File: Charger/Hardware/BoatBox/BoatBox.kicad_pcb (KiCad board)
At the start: 2 copper layers, 97.2 x 86.3 mm, 154 parts, among them P101 TestPoint, P102 TestPoint, P103 TestPoint, P104 TestPoint, P105 TestPoint, P106 TestPoint, P107 TestPoint, P108 TestPoint, P109 TestPoint, P110 TestPoint, P111 TestPoint, P112 TestPoint, P113 TestPoint, P114 TestPoint, P115 TestPoint, P116 TestPoint, P117 TestPoint, P118 TestPoint, P119 TestPoint, P120 TestPoint, P201 TestPoint, P202 TestPoint, P301 TestPoint, P302 TestPoint, P401 TestPoint, P402 TestPoint, P501 TestPoint, P502 TestPoint, T101 IRFR5505PBF, T102 BSS138, T103 IRFR5505PBF, T201 BC847, T202 IPD50R380CE, T203 BSS138, T301 BC847, T302 IPD50R380CE, T303 BSS138, T401 BC847, T402 IPD50R380CE, T403 BSS138, T501 BC847, T502 IPD50R380CE, T503 BSS138, X101 HCCPHPE24BKA90F

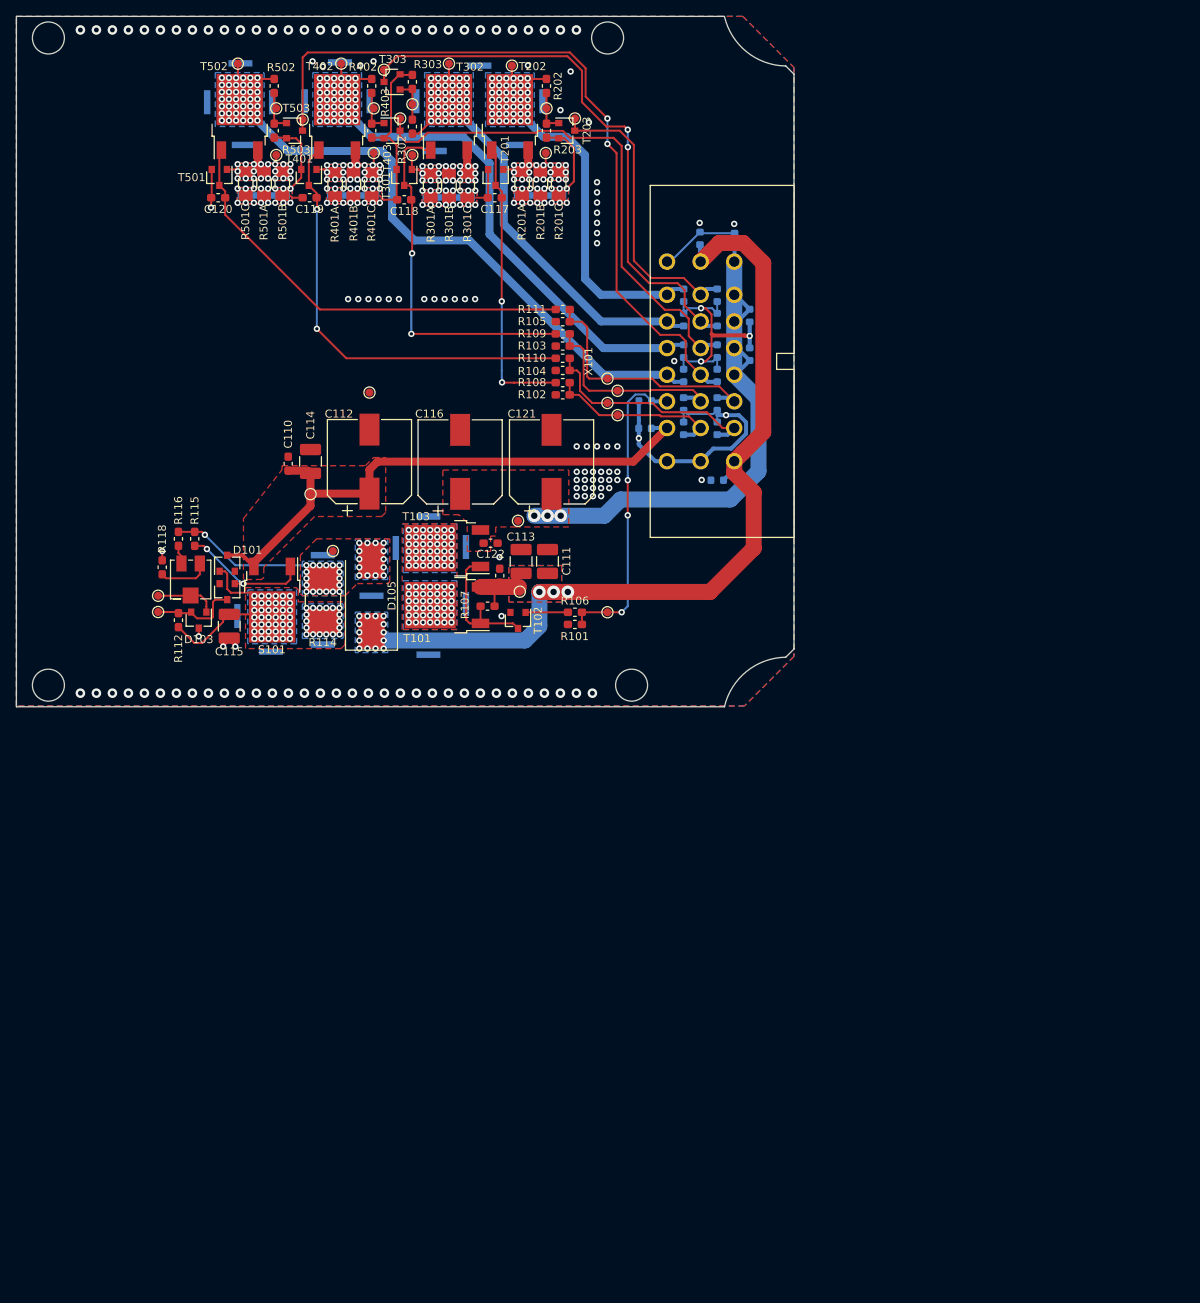
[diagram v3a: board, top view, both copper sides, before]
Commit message: Start to create the new pcb
Main features in this revision shall be:
 -) 3D printed housing
 -) raised aluminium inlay for heat transfer
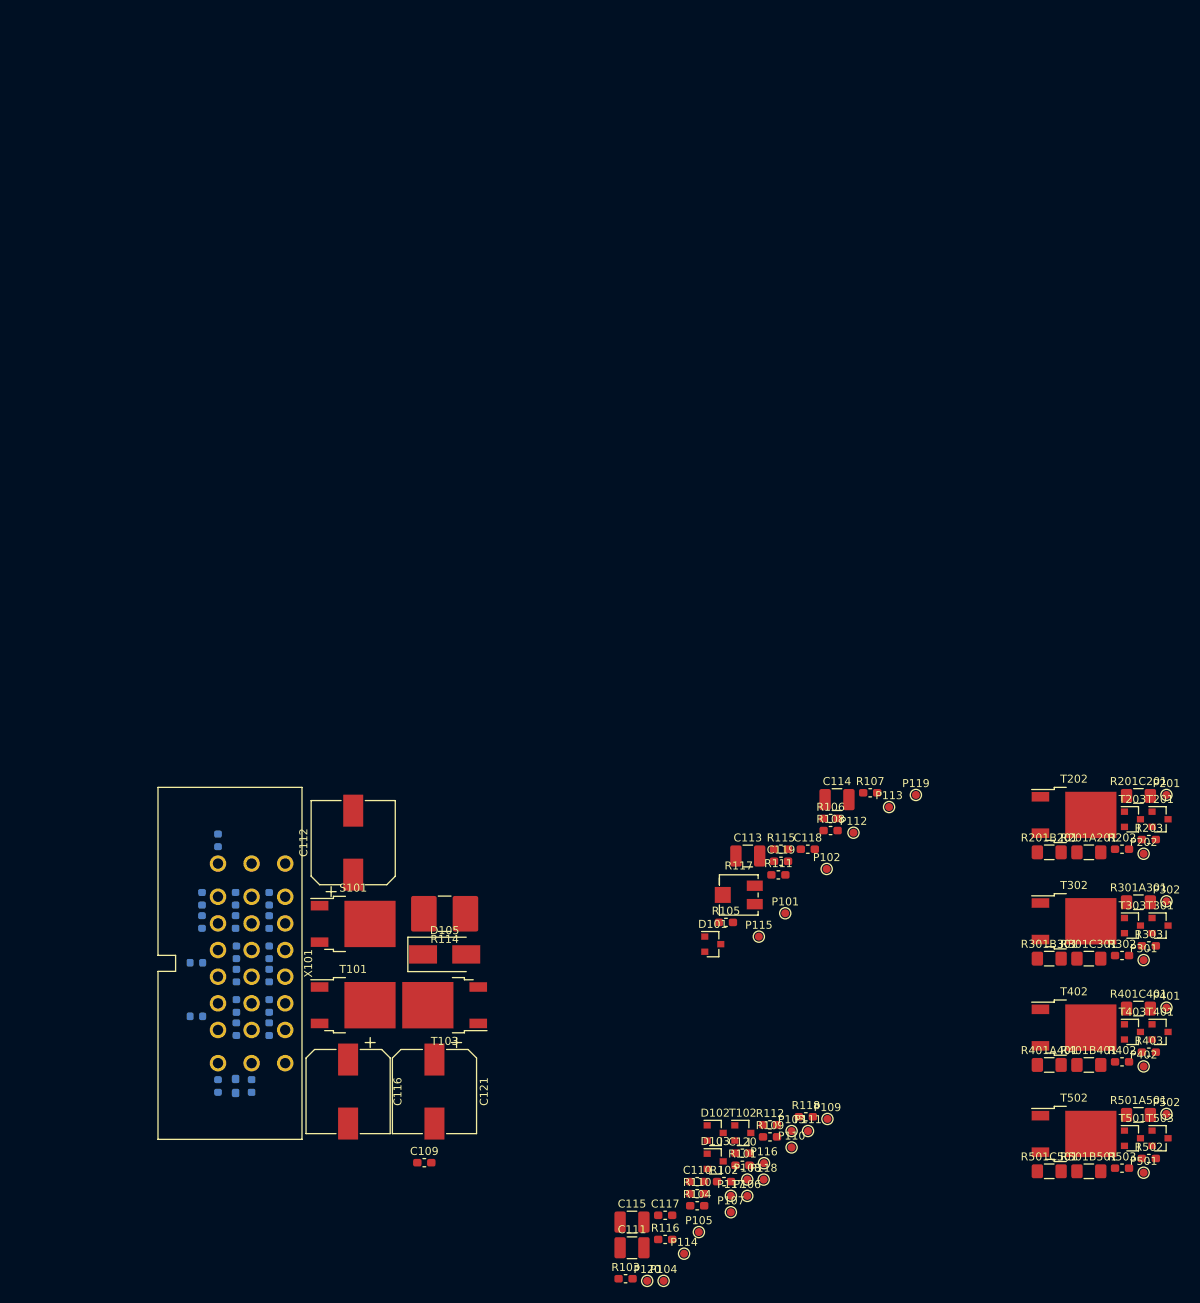
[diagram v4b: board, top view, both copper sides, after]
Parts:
- removed ?: , boatbox:Zeichnung
- removed C101, C102, C103, C104, C105, C106, C107, C108, C124, C125, C126, C127, C128, C129, C130, C131, C132, C133, C134: 4.7n, Capacitor_SMD:C_0603_1608Metric
- removed R201A, R201B, R201C, R301A, R301B, R301C, R401A, R401B, R401C, R501A, R501B, R501C: 1R, Resistor_SMD:R_1206_3216Metric_Pad1.42x1.75mm_HandSolder
- removed REF** (x30): BUMP-SR0.8-3.0, boatbox:BUMP-SR0.8-3.0
- removed REF** (x4): MountingHole_4mm, MountingHole:MountingHole_4mm
- added C0A1: 4.7n, Capacitor_SMD:C_0603_1608Metric, B.Cu at (186.2, 169.4)
- added C0A2: 4.7n, Capacitor_SMD:C_0603_1608Metric, B.Cu at (184.2, 176.7)
- added C0A3: 4.7n, Capacitor_SMD:C_0603_1608Metric, B.Cu at (184.2, 179.6)
- added C0A5: 4.7n, Capacitor_SMD:C_0603_1608Metric, B.Cu at (183.5, 184.7)
- added C0A7: 4.7n, Capacitor_SMD:C_0603_1608Metric, B.Cu at (183.5, 191.4)
- added C0A8: 4.7n, Capacitor_SMD:C_0603_1608Metric, B.Cu at (186.2, 200.1)
- added C0B2: 4.7n, Capacitor_SMD:C_0603_1608Metric, B.Cu at (188.4, 176.7)
- added C0B3: 4.7n, Capacitor_SMD:C_0603_1608Metric, B.Cu at (188.4, 179.6)
- added C0B4: 4.7n, Capacitor_SMD:C_0603_1608Metric, B.Cu at (188.5, 183.4)
- added C0B5: 4.7n, Capacitor_SMD:C_0603_1608Metric, B.Cu at (188.5, 186.3)
- added C0B6: 4.7n, Capacitor_SMD:C_0603_1608Metric, B.Cu at (188.5, 190.1)
- added C0B7: 4.7n, Capacitor_SMD:C_0603_1608Metric, B.Cu at (188.5, 193.0)
- added C0B8: 4.7n, Capacitor_SMD:C_0603_1608Metric, B.Cu at (190.4, 200.1)
- added C0C2: 4.7n, Capacitor_SMD:C_0603_1608Metric, B.Cu at (192.6, 176.7)
- added C0C3: 4.7n, Capacitor_SMD:C_0603_1608Metric, B.Cu at (192.6, 179.6)
- added C0C4: 4.7n, Capacitor_SMD:C_0603_1608Metric, B.Cu at (192.6, 183.4)
- added C0C5: 4.7n, Capacitor_SMD:C_0603_1608Metric, B.Cu at (192.6, 186.3)
- added C0C6: 4.7n, Capacitor_SMD:C_0603_1608Metric, B.Cu at (192.6, 190.1)
- added C0C7: 4.7n, Capacitor_SMD:C_0603_1608Metric, B.Cu at (192.6, 193.0)
- added R201A201: 1R, Resistor_SMD:R_1206_3216Metric_Pad1.42x1.75mm_HandSolder, F.Cu at (295.0, 170.9)
- added R201B201: 1R, Resistor_SMD:R_1206_3216Metric_Pad1.42x1.75mm_HandSolder, F.Cu at (290.1, 170.9)
- added R201C201: 1R, Resistor_SMD:R_1206_3216Metric_Pad1.42x1.75mm_HandSolder, F.Cu at (301.2, 163.8)
- added R301A301: 1R, Resistor_SMD:R_1206_3216Metric_Pad1.42x1.75mm_HandSolder, F.Cu at (301.2, 177.1)
- added R301B301: 1R, Resistor_SMD:R_1206_3216Metric_Pad1.42x1.75mm_HandSolder, F.Cu at (290.1, 184.1)
- added R301C301: 1R, Resistor_SMD:R_1206_3216Metric_Pad1.42x1.75mm_HandSolder, F.Cu at (295.0, 184.1)
- added R401A401: 1R, Resistor_SMD:R_1206_3216Metric_Pad1.42x1.75mm_HandSolder, F.Cu at (290.1, 197.4)
- added R401B401: 1R, Resistor_SMD:R_1206_3216Metric_Pad1.42x1.75mm_HandSolder, F.Cu at (295.0, 197.4)
- added R401C401: 1R, Resistor_SMD:R_1206_3216Metric_Pad1.42x1.75mm_HandSolder, F.Cu at (301.2, 190.4)
- added R501A501: 1R, Resistor_SMD:R_1206_3216Metric_Pad1.42x1.75mm_HandSolder, F.Cu at (301.2, 203.7)
- added R501B501: 1R, Resistor_SMD:R_1206_3216Metric_Pad1.42x1.75mm_HandSolder, F.Cu at (295.0, 210.7)
- added R501C501: 1R, Resistor_SMD:R_1206_3216Metric_Pad1.42x1.75mm_HandSolder, F.Cu at (290.1, 210.7)
- C122: moved to B.Cu
- D105: footprint Diode_SMD:D_SMC_Handsoldering -> Diode_SMD:D_SMB_Handsoldering
- moved R502 173.0 mm to (302.5, 209.1), turned to 0 degrees
- moved P502 167.9 mm to (304.7, 203.6), turned to 0 degrees
- moved R503 167.5 mm to (299.2, 210.3), turned to 0 degrees
- moved P501 167.1 mm to (301.9, 210.9), turned to 0 degrees
- moved T503 166.0 mm to (303.9, 206.6)
- moved T501 165.7 mm to (300.5, 206.6), turned to 0 degrees
- moved T502 164.5 mm to (293.2, 206.1), turned to 0 degrees
- moved P120 160.5 mm to (239.8, 224.4), turned to 0 degrees
- moved R402 153.9 mm to (299.2, 197.0), turned to 0 degrees
- moved P402 153.6 mm to (301.9, 197.6), turned to 0 degrees
- moved T401 150.8 mm to (303.9, 193.3), turned to 0 degrees
- moved R403 150.7 mm to (302.5, 195.8), turned to 0 degrees
- moved P114 150.1 mm to (244.4, 221.0), turned to 0 degrees
- moved P118 149.2 mm to (254.4, 211.8), turned to 0 degrees
- moved T402 146.5 mm to (293.2, 192.8), turned to 0 degrees
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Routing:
- net GND: track 134.5 -> 0.00 mm, vias 198 -> 0
- net UBD: track 120.2 -> 0.00 mm, vias 17 -> 0
- net /A_S_DIAG4: track 93.7 -> 0.00 mm, vias 2 -> 0
- net /A_T_OUT4: track 77.7 -> 0.00 mm, vias 42 -> 0
- net /U_U_CHRG: track 73.2 -> 0.00 mm
- net /A_S_DIAG2: track 71.0 -> 0.00 mm, vias 2 -> 0
- net UBR: track 70.3 -> 0.00 mm, vias 3 -> 0
- net /A_S_DIAG3: track 64.2 -> 0.00 mm
- net /A_T_OUT3: track 62.1 -> 0.00 mm, vias 42 -> 0
- net /LSS 3/ctrl: track 54.8 -> 0.00 mm, vias 2 -> 0
- net /LSS 4/ctrl: track 54.7 -> 0.00 mm
- net /A_T_OUT1: track 48.2 -> 0.00 mm, vias 42 -> 0
- net /A_T_OUT2: track 47.6 -> 0.00 mm, vias 42 -> 0
- net /LSS 2/ctrl: track 45.5 -> 0.00 mm, vias 2 -> 0
- net /E_S_RLY: track 38.7 -> 0.00 mm, vias 3 -> 0
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- removed copper zone on B.Cu, net /A_T_OUT1
- removed copper zone on B.Cu, net /A_T_OUT2
- removed copper zone on B.Cu, net /A_T_OUT3
- removed copper zone on B.Cu, net /A_T_OUT4
- removed copper zone on F.Cu, net /U_U_CHRG
- removed copper zone on B.Cu, net GND
- removed copper zone on F.Cu, net GND
- removed copper zone on B.Cu, net Net-(C115-Pad1)
- removed copper zone on F.Cu, net Net-(C115-Pad1)
- removed copper zone on B.Cu, net Net-(D105-Pad2)
- removed copper zone on F.Cu, net Net-(D105-Pad2)
- removed copper zone on B.Cu, net Net-(P201-Pad1)
- removed copper zone on F.Cu, net Net-(P201-Pad1)
- removed copper zone on B.Cu, net Net-(P301-Pad1)
- removed copper zone on F.Cu, net Net-(P301-Pad1)
- removed copper zone on B.Cu, net Net-(P401-Pad1)
- removed copper zone on F.Cu, net Net-(P401-Pad1)
- removed copper zone on B.Cu, net Net-(P501-Pad1)
- removed copper zone on F.Cu, net Net-(P501-Pad1)
- removed copper zone on B.Cu, net Net-(T101-Pad2)
- removed copper zone on F.Cu, net Net-(T101-Pad2)
- removed copper zone on B.Cu, net UBD
- removed copper zone on F.Cu, net UBD
- removed copper zone on F.Cu, net UBR
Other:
- board outline removed

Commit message: WIP commit of new layout
squash after finish
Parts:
- added REF**: MountingHole_3.2mm_M3_Pad_Via, MountingHole:MountingHole_3.2mm_M3_Pad_Via, F.Cu at (245.0, 211.0)
- added REF**: MountingHole_3.2mm_M3_Pad_Via, MountingHole:MountingHole_3.2mm_M3_Pad_Via, F.Cu at (245.0, 159.0)
- added REF**: MountingHole_3.2mm_M3_Pad_Via, MountingHole:MountingHole_3.2mm_M3_Pad_Via, F.Cu at (183.0, 211.0)
- added REF**: MountingHole_3.2mm_M3_Pad_Via, MountingHole:MountingHole_3.2mm_M3_Pad_Via, F.Cu at (184.0, 159.0)
- C109, C110, R101, R106: moved to B.Cu
- moved P502 87.9 mm to (221.4, 175.6), turned to 270 degrees
- moved T503 87.4 mm to (223.0, 173.6), turned to 180 degrees
- moved T201 86.3 mm to (224.7, 200.8), turned to 180 degrees
- moved T501 85.7 mm to (223.0, 169.9), turned to 180 degrees
- moved R502 83.3 mm to (227.2, 173.6), turned to 270 degrees
- moved R503 82.3 mm to (225.6, 173.6), turned to 90 degrees
- moved R203 81.7 mm to (229.0, 204.8), turned to 270 degrees
- moved P202 81.3 mm to (227.2, 203.3), turned to 90 degrees
- moved P201 79.6 mm to (232.3, 196.7), turned to 90 degrees
- moved T203 78.8 mm to (231.5, 204.8)
- moved P501 77.3 mm to (229.5, 183.9), turned to 270 degrees
- moved R202 76.8 mm to (229.0, 201.5), turned to 270 degrees
- moved R107 72.6 mm to (200.7, 191.5), turned to 270 degrees
- moved R201C201 72.5 mm to (234.8, 193.0), turned to 90 degrees
- moved R401C401 72.5 mm to (230.5, 174.6), turned to 270 degrees
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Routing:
- net UBD: track 0.00 -> 91.4 mm
- net UBR: track 0.00 -> 91.1 mm, vias 0 -> 2
- net /A_T_OUT3: track 0.00 -> 67.5 mm, vias 0 -> 1
- net /A_T_OUT2: track 0.00 -> 64.3 mm
- net /A_T_OUT1: track 0.00 -> 45.5 mm, vias 0 -> 1
- net /U_U_CHRG: track 0.00 -> 38.6 mm, vias 0 -> 1
- net /A_T_OUT4: track 0.00 -> 36.1 mm
- net Net-(R107-Pad1): track 0.00 -> 29.5 mm
- net Net-(P501-Pad1): track 0.00 -> 28.4 mm, vias 0 -> 2
- net GND: track 0.00 -> 25.9 mm
- net /LSS 4/ctrl: track 0.00 -> 20.9 mm, vias 0 -> 2
- net /LSS 2/ctrl: track 0.00 -> 20.2 mm
- net Net-(R106-Pad2): track 0.00 -> 17.8 mm, vias 0 -> 3
- net Net-(P301-Pad1): track 0.00 -> 10.3 mm
- net /LSS 1/ctrl: track 0.00 -> 9.85 mm
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- added copper zone on B.Cu, net Net-(T101-Pad2)
- added copper zone on F.Cu, net Net-(T101-Pad2)
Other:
- board outline added: 70 x 60 mm

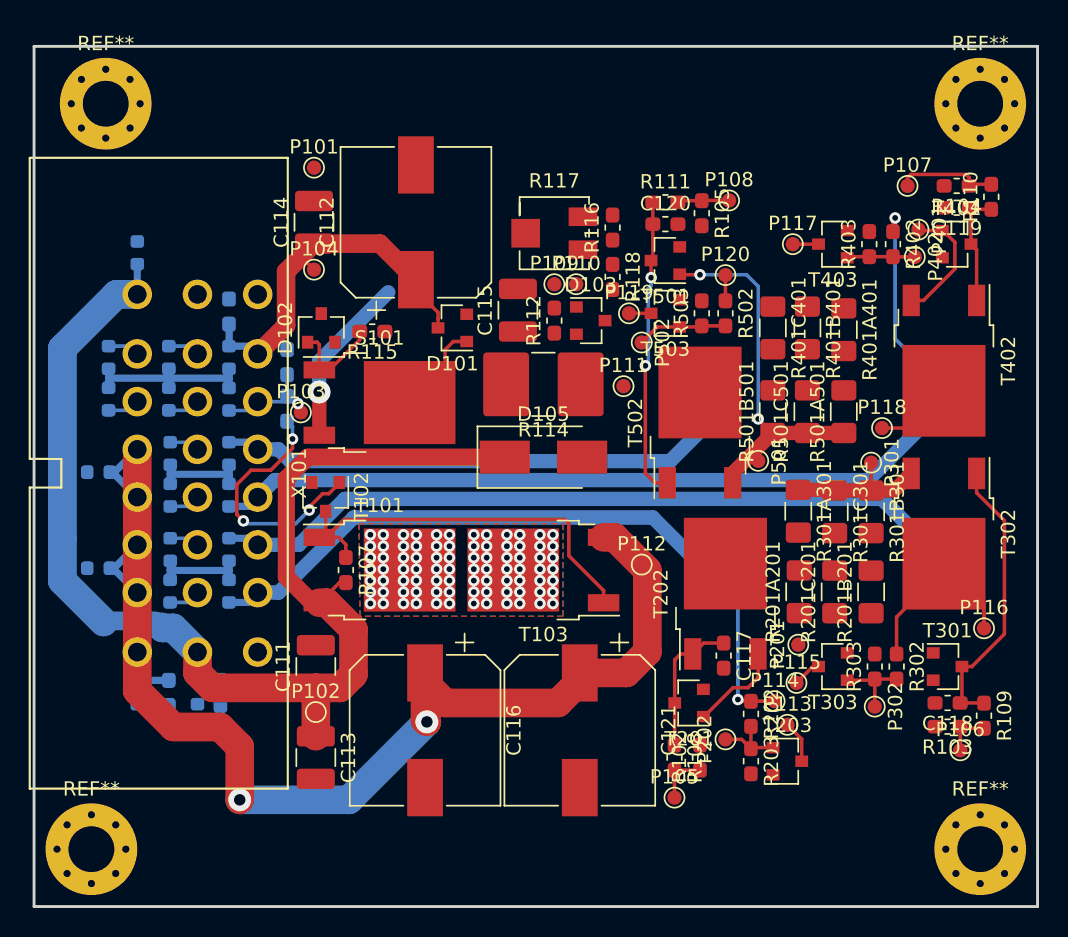
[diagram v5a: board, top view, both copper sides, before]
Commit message: New layout finished
Started work on the 3D printed housing. The cooling bench will be created
as an inlay made of 4mm steel (or aluminium).
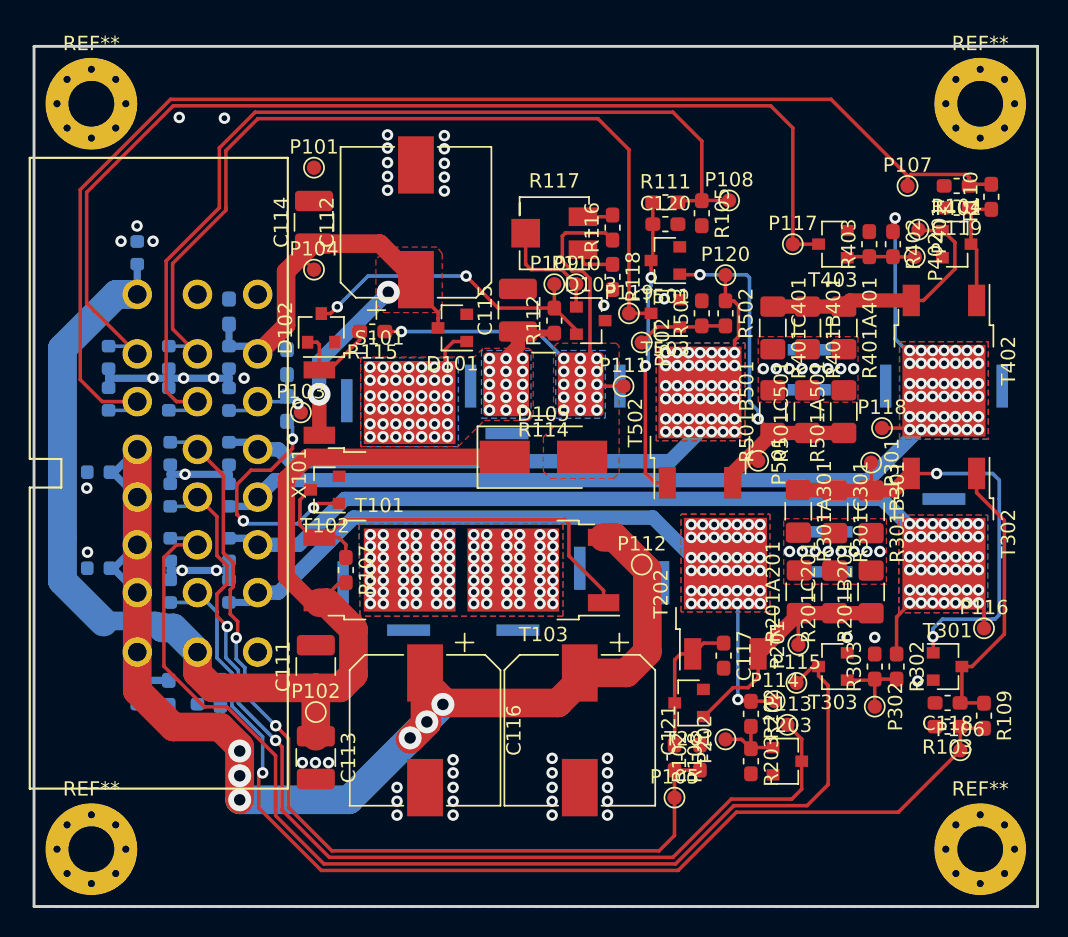
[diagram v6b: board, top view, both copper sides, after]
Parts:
- added REF**: BUMP-SR0.8-3.0, boatbox:BUMP-SR0.8-3.0, B.Cu at (200.5, 192.4)
- added REF**: BUMP-SR0.8-3.0, boatbox:BUMP-SR0.8-3.0, B.Cu at (217.1, 191.4)
- added REF**: BUMP-SR0.8-3.0, boatbox:BUMP-SR0.8-3.0, B.Cu at (233.1, 176.1)
- added REF**: BUMP-SR0.8-3.0, boatbox:BUMP-SR0.8-3.0, B.Cu at (233.1, 178.9)
- added REF**: BUMP-SR0.8-3.0, boatbox:BUMP-SR0.8-3.0, B.Cu at (234.6, 188.8)
- added REF**: BUMP-SR0.8-3.0, boatbox:BUMP-SR0.8-3.0, B.Cu at (234.6, 191.6)
- added REF**: BUMP-SR0.8-3.0, boatbox:BUMP-SR0.8-3.0, B.Cu at (222.9, 192.4)
- added REF**: BUMP-SR0.8-3.0, boatbox:BUMP-SR0.8-3.0, B.Cu at (242.5, 186.5)
- added REF**: BUMP-SR0.8-3.0, boatbox:BUMP-SR0.8-3.0, B.Cu at (238.4, 178.7)
- added REF**: BUMP-SR0.8-3.0, boatbox:BUMP-SR0.8-3.0, B.Cu at (246.5, 178.7)
- added REF**: BUMP-SR0.8-3.0, boatbox:BUMP-SR0.8-3.0, B.Cu at (209.4, 178.7)
- added REF**: BUMP-SR0.8-3.0, boatbox:BUMP-SR0.8-3.0, B.Cu at (212.0, 182.0)
- added REF**: BUMP-SR0.8-3.0, boatbox:BUMP-SR0.8-3.0, B.Cu at (219.8, 178.7)
- added REF**: BUMP-SR0.8-3.0, boatbox:BUMP-SR0.8-3.0, B.Cu at (200.8, 179.7)
- added REF**: BUMP-SR0.8-3.0, boatbox:BUMP-SR0.8-3.0, B.Cu at (212.7, 195.7)
- added REF**: BUMP-SR0.8-3.0, boatbox:BUMP-SR0.8-3.0, B.Cu at (205.1, 195.7)
- moved REF** 1.00 mm to (183.0, 159.0)
- moved T102 0.49 mm to (199.3, 185.9), turned to 180 degrees
- moved R401A401 0.13 mm to (235.5, 174.6)
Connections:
- C0A2 pad 2: /E_S_CTL3 -> /A_S_DIAG3
- C0A3 pad 2: /E_S_CTL4 -> /E_S_CTL3
- C0B2 pad 2: /E_S_CTL1 -> /A_S_DIAG4
- C0B3 pad 2: /E_S_CTL2 -> /E_S_CTL4
- C0B4 pad 2: /A_S_DIAG4 -> /E_S_CTL1
- C0B5 pad 2: /A_S_DIAG3 -> /A_S_DIAG1
- C0B7 pad 2: /A_S_DIAG1 -> /E_S_CTL2
- X101 pad 10: /E_S_CTL1 -> /A_S_DIAG4
- X101 pad 11: /E_S_CTL2 -> /E_S_CTL4
- X101 pad 12: /A_S_DIAG4 -> /E_S_CTL1
- X101 pad 13: /A_S_DIAG3 -> /A_S_DIAG1
- X101 pad 15: /A_S_DIAG1 -> /E_S_CTL2
- X101 pad 2: /E_S_CTL3 -> /A_S_DIAG3
- X101 pad 3: /E_S_CTL4 -> /E_S_CTL3
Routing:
- net /E_S_CTL3: track 9.44 -> 90.6 mm
- net /A_S_DIAG2: track 4.10 -> 79.7 mm
- net /A_S_DIAG3: track 3.96 -> 77.2 mm
- net /E_S_CTL2: track 5.62 -> 76.4 mm, vias 0 -> 1
- net /A_S_DIAG1: track 5.14 -> 71.6 mm, vias 0 -> 2
- net /E_S_CTL4: track 5.87 -> 66.5 mm
- net /E_S_CTL1: track 5.92 -> 64.9 mm, vias 0 -> 2
- net /A_S_DIAG4: track 3.65 -> 61.6 mm
- net Net-(D105-Pad2): track 0.00 -> 28.9 mm, vias 0 -> 16
- net Net-(P301-Pad1): track 10.3 -> 32.8 mm, vias 0 -> 2
- net Net-(D102-Pad1): track 0.00 -> 22.4 mm, vias 0 -> 2
- net Net-(P201-Pad1): track 6.60 -> 17.9 mm
- net Net-(P401-Pad1): track 8.72 -> 18.6 mm
- net Net-(D103-Pad1): track 0.00 -> 7.86 mm
- net UBR: track 91.1 -> 97.9 mm, vias 2 -> 6
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- added copper zone on B.Cu, net /A_T_OUT1
- added copper zone on F.Cu, net /A_T_OUT1
- added copper zone on B.Cu, net /A_T_OUT2
- added copper zone on F.Cu, net /A_T_OUT2
- added copper zone on B.Cu, net /A_T_OUT3
- added copper zone on F.Cu, net /A_T_OUT3
- added copper zone on B.Cu, net /A_T_OUT4
- added copper zone on F.Cu, net /A_T_OUT4
- added copper zone on F.Cu, net /U_U_CHRG
- added copper zone on B.Cu, net GND
- added copper zone on F.Cu, net GND
- added copper zone on B.Cu, net Net-(C115-Pad1)
- added copper zone on F.Cu, net Net-(C115-Pad1)
- added copper zone on B.Cu, net Net-(D105-Pad2)
- added copper zone on F.Cu, net Net-(D105-Pad2)
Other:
- net class 3A: clearance 0.3 -> 0.2
- net class 6A: clearance 0.3 -> 0.2
